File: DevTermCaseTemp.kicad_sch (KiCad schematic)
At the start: 91 parts, among them J1 USB_A, J11 Conn_01x06, J2 EXT_miniPCIe, J3 USB_A, J4 USB_B_Micro, J5 Conn_01x02, J7 DevTermSpeaker, J8 DevTermSpeaker, J9 Conn_02x22_Odd_Even, M1 CBM-40C Series Fan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

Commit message: Replaced ESD surge diodes with USBLC6
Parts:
- removed D1, D10, D11, D12, D13, D14, D15, D16, D17, D18, D19, D2, D3, D4, D5, D6, D9: ESD, Diode_SMD:D_SOD-323, symbol Diode:ESD9B5.0ST5G
- removed M1: CBM-40C Series Fan, devterm-ext-outline:CBM-40C-Series-Fan, symbol devterm_symbols:DevTermFan3505
- added U13, U14, U15, U16, U17, U18: USBLC6-2P6, Package_TO_SOT_SMD:SOT-666, symbol Power_Protection:USBLC6-2P6
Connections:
- net +5VP: now also U14.5 (VBUS), U15.5 (VBUS), U16.5 (VBUS), U17.5 (VBUS), U18.5 (VBUS)
- net EXT_USB1.D+: now also U16.4 (I/O2); no longer U1.28
- net EXT_USB1.D-: now also U16.6 (I/O1); no longer U1.27
- net EXT_USB2.D+: now also U17.6 (I/O1); no longer U1.3
- net EXT_USB2.D-: now also U17.4 (I/O2); no longer U1.2
- net EXT_USB3.D+: now also U18.6 (I/O1); no longer U1.9
- net EXT_USB3.D-: now also U18.4 (I/O2); no longer U1.8
- net EXT_USB4.D+: now also U14.6 (I/O1); no longer J1.3 (D+)
- net EXT_USB4.D-: now also U14.4 (I/O2); no longer J1.2 (D-)
- net GND: now also J5.1 (Pin_1), U13.2 (GND), U14.2 (GND), U15.2 (GND), U16.2 (GND), U17.2 (GND), U18.2 (GND); no longer J5.2 (Pin_2)
- net USB3.D+: now also U15.6 (I/O1); no longer J3.3 (D+)
- net USB3.D-: now also U15.4 (I/O2); no longer J3.2 (D-)
- net VBUS: now also U13.5 (VBUS)
- net at U6.1 (UD+): now also U13.6 (I/O1); no longer J4.3 (D+)
- net at U6.2 (UD-): now also U13.4 (I/O2); no longer J4.2 (D-)
- net at U4.3 (VBAT): now also J5.2 (Pin_2); no longer J5.1 (Pin_1)
- new net: J1.2 (D-), U14.3 (I/O2)
- new net: J1.3 (D+), U14.1 (I/O1)
- new net: J4.2 (D-), U13.3 (I/O2)
- new net: J4.3 (D+), U13.1 (I/O1)
- new net: J3.3 (D+), U15.1 (I/O1)
- new net: J3.2 (D-), U15.3 (I/O2)
- new net U1.D1+: U1.28, U16.3 (I/O2)
- new net U1.D1-: U1.27, U16.1 (I/O1)
- new net U2.D+: U1.3, U17.1 (I/O1)
- new net U2.D-: U1.2, U17.3 (I/O2)
- new net U3.D+: U1.9, U18.1 (I/O1)
- new net U3.D-: U1.8, U18.3 (I/O2)

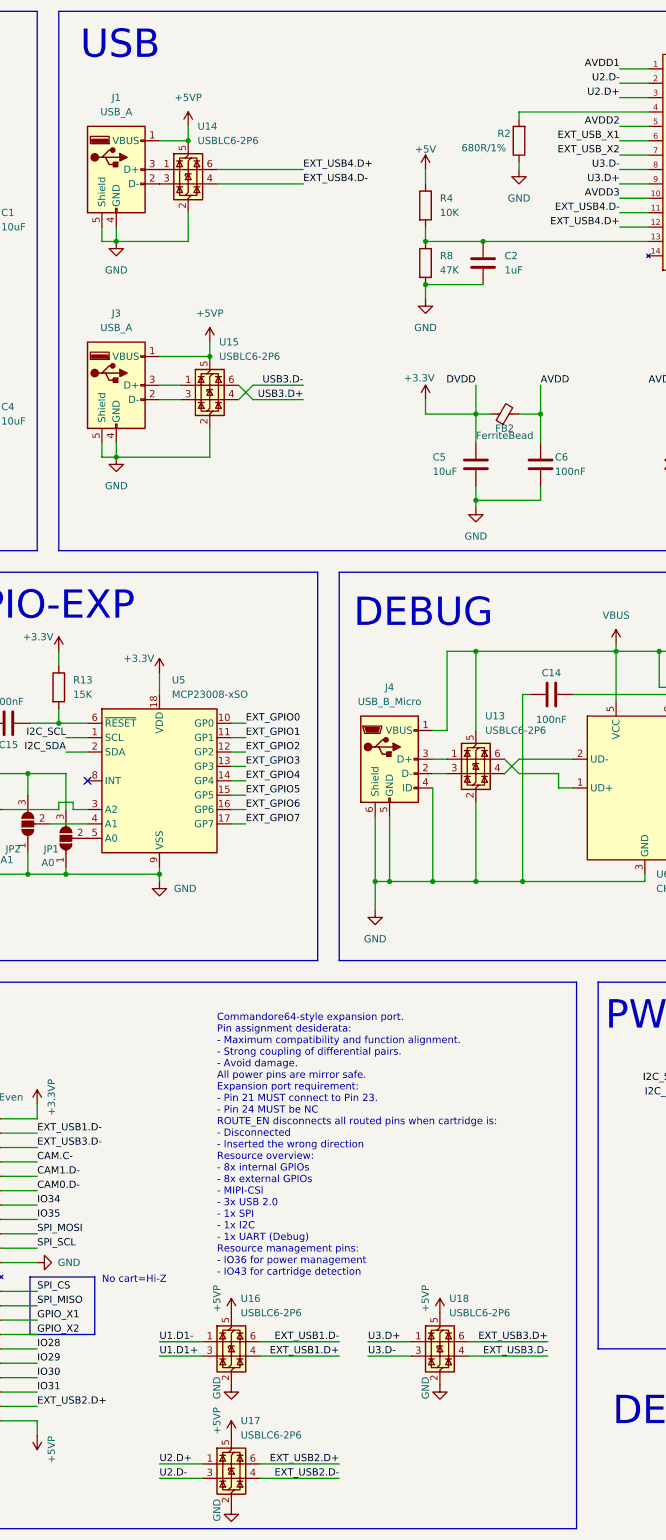
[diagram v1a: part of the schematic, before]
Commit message: Added bypass caps for USB ESD surge protection as specified in datasheet.
+ Updated silkscreen for version and serial number
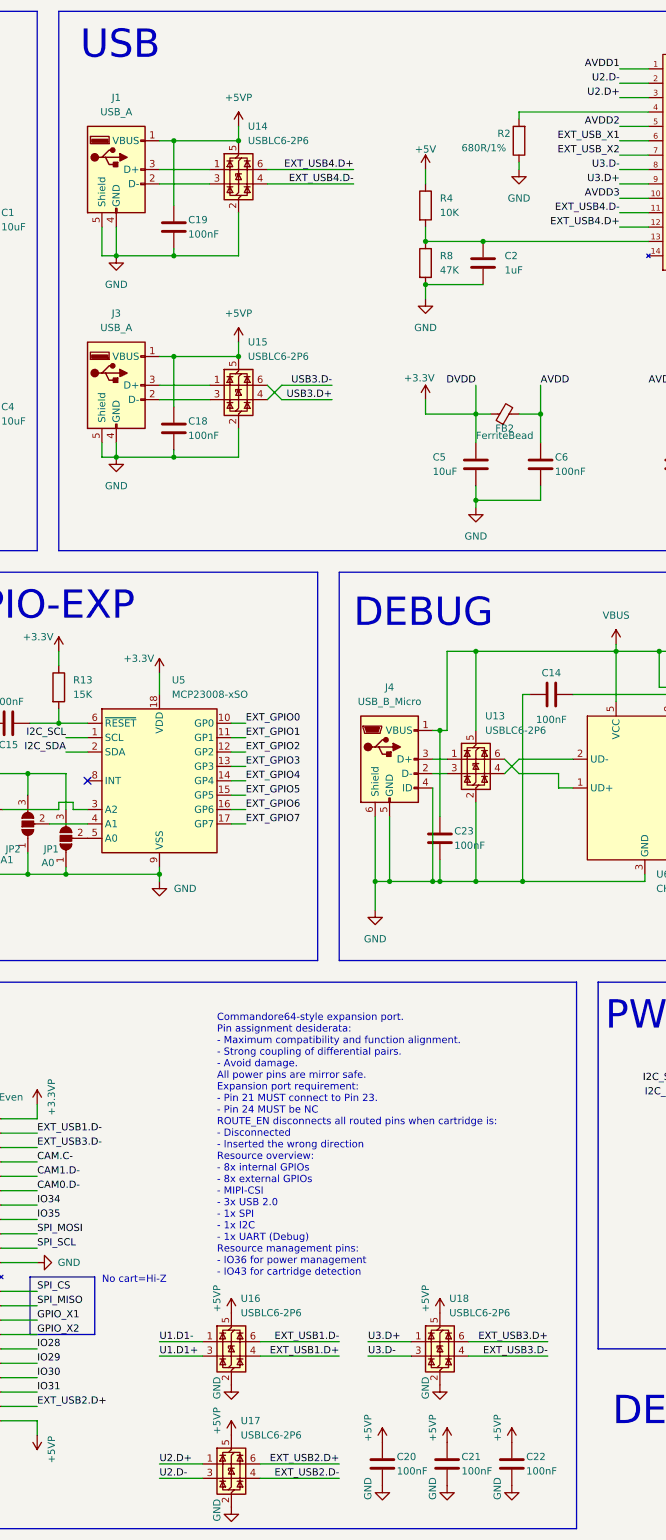
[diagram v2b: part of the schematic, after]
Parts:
- added C18, C19, C20, C21, C22, C23: 100nF, Capacitor_SMD:C_0805_2012Metric, symbol Device:C
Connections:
- net +5VP: now also C18.1, C19.1, C20.1, C21.1, C22.1
- net GND: now also C18.2, C19.2, C20.2, C21.2, C22.2, C23.2
- net VBUS: now also C23.1
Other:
- moved on the sheet: U14, U15
